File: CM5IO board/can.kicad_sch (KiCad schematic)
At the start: 0 parts

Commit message: Duplicated additional USB-C in sch.
How to change pin label on CM5?
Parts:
- added C28: 100nF, Capacitor_SMD:C_0402_1005Metric, symbol Device:C_Small
- added C29: 10uF, Capacitor_SMD:C_0402_1005Metric, symbol Device:C_Small
- added C30: 47nF, Capacitor_SMD:C_0402_1005Metric, symbol Device:C
- added D4: SM712_SOT23, Package_TO_SOT_SMD:SOT-23, symbol Diode:SM712_SOT23
- added JP1: TermJP, iclr:SmallerSolderJP, symbol Jumper:SolderJumper_2_Open
- added R21: 0, Resistor_SMD:R_0603_1608Metric, symbol Device:R_Small
- added R22, R23: 60, Resistor_SMD:R_0603_1608Metric, symbol Device:R
- added U2: SN65HVD230, Package_SO:SOIC-8_3.9x4.9mm_P1.27mm, symbol Interface_CAN_LIN:SN65HVD230
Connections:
- new net: R21.1, U2.8 (Rs)
- new net: C30.1, JP1.2 (B), R22.2, R23.1
- new net +3V3: C28.1, C29.1, U2.3 (VCC)
- new net CAN_HIGH: D4.2 (A2), R22.1, U2.7 (CANH)
- new net CAN_LOW: D4.1 (A1), R23.2, U2.6 (CANL)
- new net CAN_RX: U2.4 (R)
- new net CAN_TX: U2.1 (D)
- new net GND: C28.2, C29.2, C30.2, D4.3 (common), R21.2, U2.2 (GND)
- new net Vref: JP1.1 (A), U2.5 (Vref)

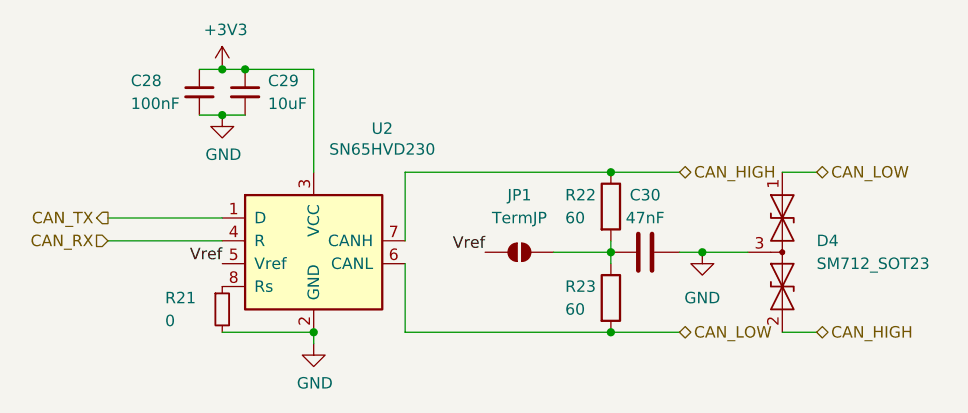
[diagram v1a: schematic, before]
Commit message: Moved Ricardo to hierarchical sheet in main sch.
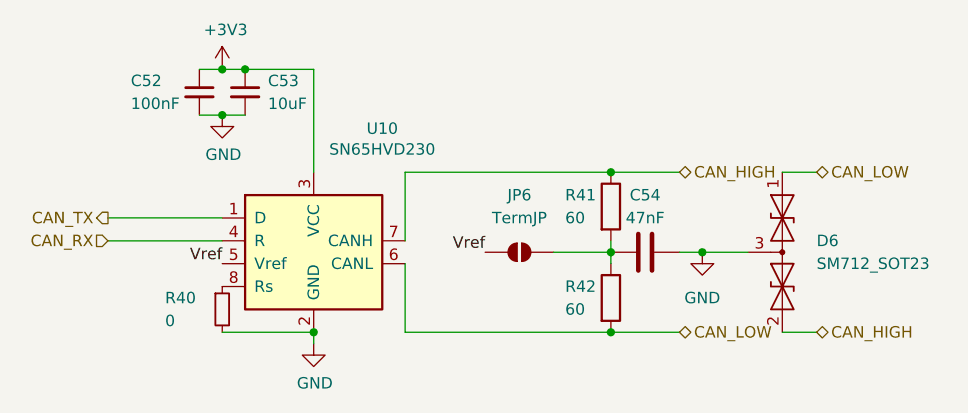
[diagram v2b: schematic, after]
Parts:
- renumbered C28 to C52, C29 to C53, C30 to C54, D4 to D6, JP1 to JP6, R21 to R40, R22 to R41, R23 to R42, U2 to U10
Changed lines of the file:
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@@
 		(dnp no)
 		(fields_autoplaced yes)
-		(property "Reference" "U2"
+		(property "Reference" "U10"
 			(at 128.27 81.5086 0)
 			(effects
@@
 		(instances
 			(project "CM5IO"
-				(path "/e63e39d7-6ac0-4ffd-8aa3-1841a4541b55/ded607f3-3cfa-4e60-bc8d-1a54579a0cf2"
-					(reference "U2")
+				(path "/e63e39d7-6ac0-4ffd-8aa3-1841a4541b55/9fe0f7c3-d1a2-46ee-9d93-86ad4b786b0e/7c83ec68-bd3c-426b-8a30-c92aec1d01ac"
+					(reference "U10")
 					(unit 1)
 				)
@@
 		(dnp no)
 		(fields_autoplaced yes)
-		(property "Reference" "#PWR052"
+		(property "Reference" "#PWR0100"
 			(at 163.83 101.6 0)
 			(effects
@@
 		(instances
 			(project "CM5IO"
-				(path "/e63e39d7-6ac0-4ffd-8aa3-1841a4541b55/ded607f3-3cfa-4e60-bc8d-1a54579a0cf2"
-					(reference "#PWR052")
+				(path "/e63e39d7-6ac0-4ffd-8aa3-1841a4541b55/9fe0f7c3-d1a2-46ee-9d93-86ad4b786b0e/7c83ec68-bd3c-426b-8a30-c92aec1d01ac"
+					(reference "#PWR0100")
 					(unit 1)
 				)
@@
 		(dnp no)
 		(fields_autoplaced yes)
-		(property "Reference" "C30"
+		(property "Reference" "C54"
 			(at 157.48 88.9 90)
 			(effects
@@
 		(instances
 			(project "CM5IO"
-				(path "/e63e39d7-6ac0-4ffd-8aa3-1841a4541b55/ded607f3-3cfa-4e60-bc8d-1a54579a0cf2"
-					(reference "C30")
+				(path "/e63e39d7-6ac0-4ffd-8aa3-1841a4541b55/9fe0f7c3-d1a2-46ee-9d93-86ad4b786b0e/7c83ec68-bd3c-426b-8a30-c92aec1d01ac"
+					(reference "C54")
 					(unit 1)
 				)
@@
 		(dnp no)
 		(fields_autoplaced yes)
-		(property "Reference" "#PWR051"
+		(property "Reference" "#PWR099"
 			(at 120.65 111.76 0)
 			(effects
@@
 		(instances
 			(project "CM5IO"
-				(path "/e63e39d7-6ac0-4ffd-8aa3-1841a4541b55/ded607f3-3cfa-4e60-bc8d-1a54579a0cf2"
-					(reference "#PWR051")
+				(path "/e63e39d7-6ac0-4ffd-8aa3-1841a4541b55/9fe0f7c3-d1a2-46ee-9d93-86ad4b786b0e/7c83ec68-bd3c-426b-8a30-c92aec1d01ac"
+					(reference "#PWR099")
 					(unit 1)
 				)
@@
 		(dnp no)
 		(fields_autoplaced yes)
-		(property "Reference" "C28"
+		(property "Reference" "C52"
 			(at 100.33 76.2 0)
 			(effects
@@
 		(instances
 			(project "CM5IO"
-				(path "/e63e39d7-6ac0-4ffd-8aa3-1841a4541b55/ded607f3-3cfa-4e60-bc8d-1a54579a0cf2"
-					(reference "C28")
+				(path "/e63e39d7-6ac0-4ffd-8aa3-1841a4541b55/9fe0f7c3-d1a2-46ee-9d93-86ad4b786b0e/7c83ec68-bd3c-426b-8a30-c92aec1d01ac"
+					(reference "C52")
 					(unit 1)
 				)
@@
 		(dnp no)
 		(fields_autoplaced yes)
-		(property "Reference" "#PWR049"
+		(property "Reference" "#PWR097"
 			(at 110.49 78.74 0)
 			(effects
@@
 		(instances
 			(project "CM5IO"
-				(path "/e63e39d7-6ac0-4ffd-8aa3-1841a4541b55/ded607f3-3cfa-4e60-bc8d-1a54579a0cf2"
-					(reference "#PWR049")
+				(path "/e63e39d7-6ac0-4ffd-8aa3-1841a4541b55/9fe0f7c3-d1a2-46ee-9d93-86ad4b786b0e/7c83ec68-bd3c-426b-8a30-c92aec1d01ac"
+					(reference "#PWR097")
 					(unit 1)
 				)
@@
 		(dnp no)
 		(fields_autoplaced yes)
-		(property "Reference" "R22"
+		(property "Reference" "R41"
 			(at 148.59 88.9 0)
 			(effects
@@
 		(instances
 			(project "CM5IO"
-				(path "/e63e39d7-6ac0-4ffd-8aa3-1841a4541b55/ded607f3-3cfa-4e60-bc8d-1a54579a0cf2"
-					(reference "R22")
+				(path "/e63e39d7-6ac0-4ffd-8aa3-1841a4541b55/9fe0f7c3-d1a2-46ee-9d93-86ad4b786b0e/7c83ec68-bd3c-426b-8a30-c92aec1d01ac"
+					(reference "R41")
 					(unit 1)
 				)
@@
 		(dnp no)
 		(fields_autoplaced yes)
-		(property "Reference" "R23"
+		(property "Reference" "R42"
 			(at 148.59 99.06 0)
 			(effects
@@
 		(instances
 			(project "CM5IO"
-				(path "/e63e39d7-6ac0-4ffd-8aa3-1841a4541b55/ded607f3-3cfa-4e60-bc8d-1a54579a0cf2"
-					(reference "R23")
+				(path "/e63e39d7-6ac0-4ffd-8aa3-1841a4541b55/9fe0f7c3-d1a2-46ee-9d93-86ad4b786b0e/7c83ec68-bd3c-426b-8a30-c92aec1d01ac"
+					(reference "R42")
 					(unit 1)
 				)
@@
 		(dnp no)
 		(fields_autoplaced yes)
-		(property "Reference" "D4"
+		(property "Reference" "D6"
 			(at 176.53 93.98 90)
 			(effects
@@
 		(instances
 			(project "CM5IO"
-				(path "/e63e39d7-6ac0-4ffd-8aa3-1841a4541b55/ded607f3-3cfa-4e60-bc8d-1a54579a0cf2"
-					(reference "D4")
+				(path "/e63e39d7-6ac0-4ffd-8aa3-1841a4541b55/9fe0f7c3-d1a2-46ee-9d93-86ad4b786b0e/7c83ec68-bd3c-426b-8a30-c92aec1d01ac"
+					(reference "D6")
 					(unit 1)
 				)
@@
 		(dnp no)
 		(fields_autoplaced yes)
-		(property "Reference" "C29"
+		(property "Reference" "C53"
 			(at 115.57 76.2062 0)
 			(effects
@@
 		(instances
 			(project "CM5IO"
-				(path "/e63e39d7-6ac0-4ffd-8aa3-1841a4541b55/ded607f3-3cfa-4e60-bc8d-1a54579a0cf2"
-					(reference "C29")
+				(path "/e63e39d7-6ac0-4ffd-8aa3-1841a4541b55/9fe0f7c3-d1a2-46ee-9d93-86ad4b786b0e/7c83ec68-bd3c-426b-8a30-c92aec1d01ac"
+					(reference "C53")
 					(unit 1)
 				)
@@
 		(dnp no)
 		(fields_autoplaced yes)
-		(property "Reference" "JP1"
+		(property "Reference" "JP6"
 			(at 143.51 88.9 0)
 			(effects
@@
 		(instances
 			(project "CM5IO"
-				(path "/e63e39d7-6ac0-4ffd-8aa3-1841a4541b55/ded607f3-3cfa-4e60-bc8d-1a54579a0cf2"
-					(reference "JP1")
+				(path "/e63e39d7-6ac0-4ffd-8aa3-1841a4541b55/9fe0f7c3-d1a2-46ee-9d93-86ad4b786b0e/7c83ec68-bd3c-426b-8a30-c92aec1d01ac"
+					(reference "JP6")
 					(unit 1)
 				)
@@
 		(on_board yes)
 		(dnp no)
-		(property "Reference" "R21"
+		(property "Reference" "R40"
 			(at 104.14 100.33 0)
 			(effects
@@
 		(instances
 			(project "CM5IO"
-				(path "/e63e39d7-6ac0-4ffd-8aa3-1841a4541b55/ded607f3-3cfa-4e60-bc8d-1a54579a0cf2"
-					(reference "R21")
+				(path "/e63e39d7-6ac0-4ffd-8aa3-1841a4541b55/9fe0f7c3-d1a2-46ee-9d93-86ad4b786b0e/7c83ec68-bd3c-426b-8a30-c92aec1d01ac"
+					(reference "R40")
 					(unit 1)
 				)
@@
 		(dnp no)
 		(fields_autoplaced yes)
-		(property "Reference" "#PWR050"
+		(property "Reference" "#PWR098"
 			(at 110.49 86.36 0)
 			(effects
@@
 		(instances
 			(project "CM5IO"
-				(path "/e63e39d7-6ac0-4ffd-8aa3-1841a4541b55/ded607f3-3cfa-4e60-bc8d-1a54579a0cf2"
-					(reference "#PWR050")
-					(unit 1)
-				)
+				(path "/e63e39d7-6ac0-4ffd-8aa3-1841a4541b55/9fe0f7c3-d1a2-46ee-9d93-86ad4b786b0e/7c83ec68-bd3c-426b-8a30-c92aec1d01ac"
+					(reference "#PWR098")
+					(unit 1)
+				)
